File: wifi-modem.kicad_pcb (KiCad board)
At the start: 2 copper layers, 63.9 x 81.7 mm, 48 parts, among them J1 RS232, J2 Power, J3 Speaker, SW1 RESET, SW2 PROG, U1 ESP-12F, U2 MAX3238EAIT, U3 AMS1117-3.3

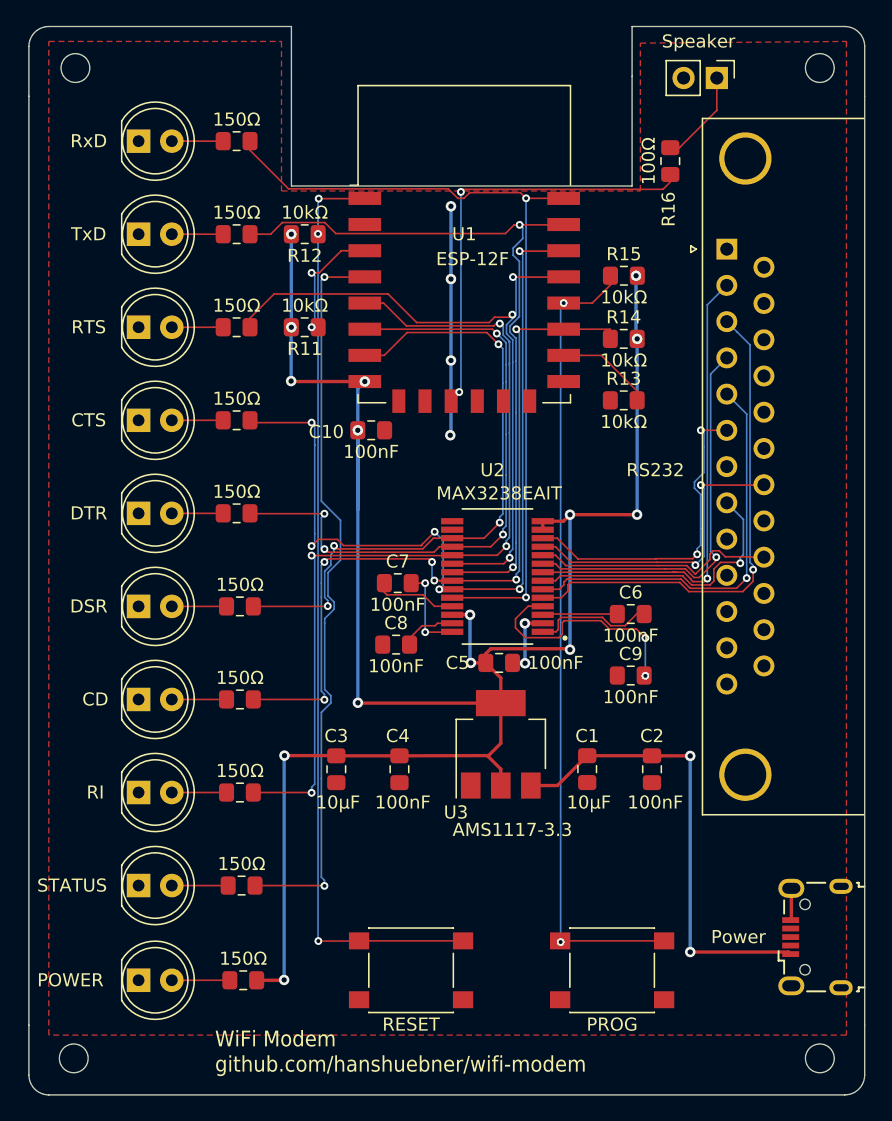
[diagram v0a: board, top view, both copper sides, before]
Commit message: Added LED drivers
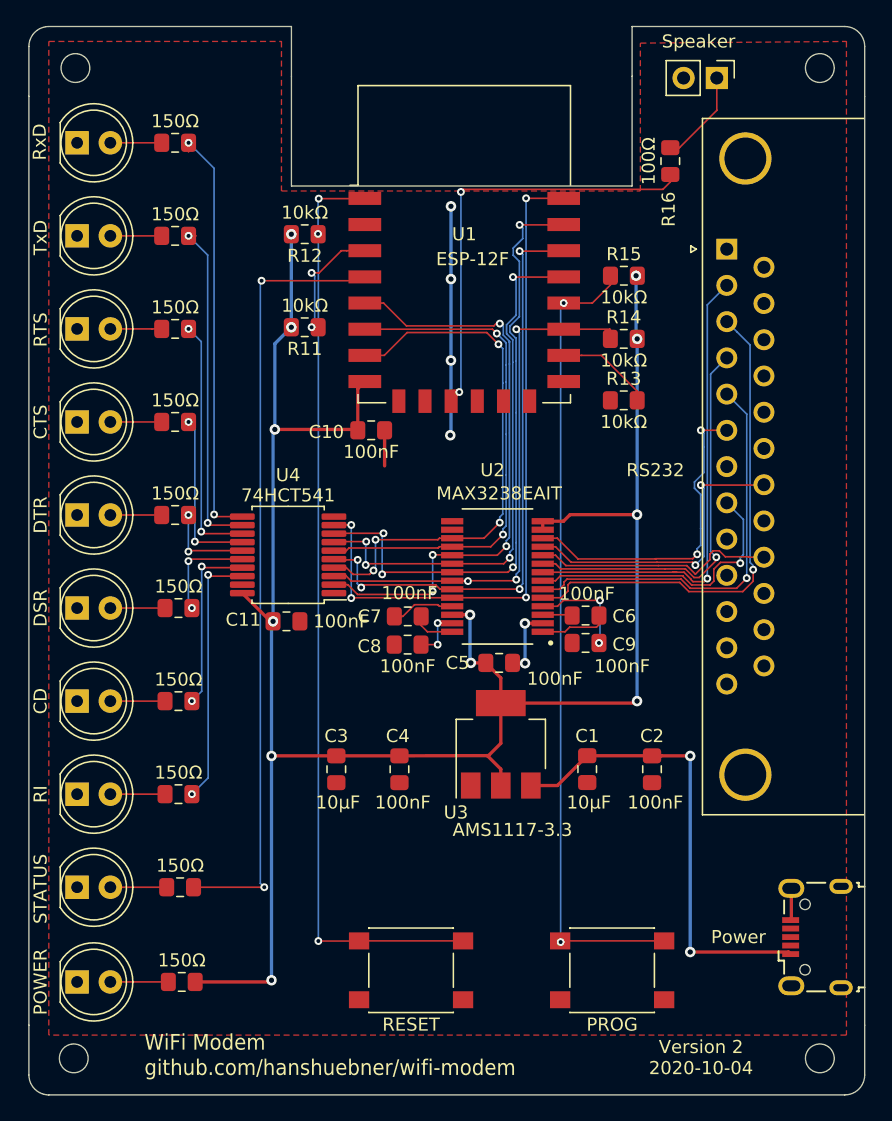
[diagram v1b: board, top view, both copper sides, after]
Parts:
- added C11: 100nF, Capacitor_SMD:C_0805_2012Metric_Pad1.15x1.40mm_HandSolder, F.Cu at (135.0, 105.0)
- added U4: 74HCT541, Package_SO:SSOP-20_5.3x7.2mm_P0.65mm, F.Cu at (135.1, 99.9)
- moved R10 4.70 mm to (127.0, 132.6)
- moved D1 4.70 mm to (119.0, 68.5)
- moved D2 4.70 mm to (119.0, 75.6)
- moved D3 4.70 mm to (119.0, 82.7)
- moved D4 4.70 mm to (119.0, 89.8)
- moved D5 4.70 mm to (119.0, 96.9)
- moved D6 4.70 mm to (119.0, 104.0)
- moved D7 4.70 mm to (119.0, 111.1)
- moved D8 4.70 mm to (119.0, 118.2)
- moved D9 4.70 mm to (119.0, 125.3)
- moved R1 4.70 mm to (126.5, 68.5)
- moved R2 4.70 mm to (126.5, 75.6)
- moved R3 4.70 mm to (126.5, 82.7)
- moved R4 4.70 mm to (126.5, 89.8)
- moved R5 4.70 mm to (126.5, 96.9)
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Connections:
- R7 pad 1: Net-(R14-Pad1) -> Net-(R7-Pad1)
- U1 pad 19: Net-(R3-Pad1) -> Net-(U1-Pad19)
- U1 pad 20: Net-(R4-Pad1) -> Net-(U1-Pad20)
- U1 pad 21: Net-(R2-Pad1) -> Net-(U1-Pad21)
- U1 pad 22: Net-(R1-Pad1) -> Net-(U1-Pad22)
- U1 pad 5: Net-(R8-Pad1) -> Net-(U1-Pad5)
- U1 pad 6: Net-(R5-Pad1) -> Net-(U1-Pad6)
- U1 pad 7: Net-(R6-Pad1) -> Net-(U1-Pad7)
- U2 pad 17: Net-(R6-Pad1) -> Net-(U1-Pad7)
- U2 pad 18: Net-(R5-Pad1) -> Net-(U1-Pad6)
- U2 pad 19: Net-(R8-Pad1) -> Net-(U1-Pad5)
- U2 pad 20: Net-(R3-Pad1) -> Net-(U1-Pad19)
- U2 pad 21: Net-(R2-Pad1) -> Net-(U1-Pad21)
- U2 pad 23: Net-(R4-Pad1) -> Net-(U1-Pad20)
- U2 pad 24: Net-(R1-Pad1) -> Net-(U1-Pad22)
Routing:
- net Net-(U1-Pad22): track 0.00 -> 53.7 mm, vias 0 -> 4
- net Net-(R4-Pad1): track 65.1 -> 13.2 mm, vias 6 -> 2
- net Net-(U1-Pad21): track 0.00 -> 48.0 mm, vias 0 -> 4
- net Net-(R8-Pad1): track 66.7 -> 19.9 mm, vias 4 -> 2
- net Net-(U1-Pad20): track 0.00 -> 45.8 mm, vias 0 -> 4
- net Net-(U1-Pad5): track 0.00 -> 45.3 mm, vias 0 -> 4
- net Net-(R5-Pad1): track 49.0 -> 6.98 mm, vias 4 -> 2
- net Net-(R6-Pad1): track 49.5 -> 7.88 mm, vias 4 -> 2
- net Net-(U1-Pad19): track 0.00 -> 41.6 mm, vias 0 -> 4
- net Net-(U1-Pad7): track 0.00 -> 41.0 mm, vias 0 -> 4
- net Net-(U1-Pad6): track 0.00 -> 39.4 mm, vias 0 -> 2
- net Net-(R3-Pad1): track 53.3 -> 19.1 mm, vias 3 -> 2
- net Net-(R2-Pad1): track 57.7 -> 25.8 mm
- net Net-(R1-Pad1): track 62.7 -> 32.1 mm
- net Net-(R14-Pad1): track 59.6 -> 42.6 mm, vias 6 -> 3
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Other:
- board text added: "Version 2 2020-10-04"

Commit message: PCB Version 3
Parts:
- added C12: 100nF, Capacitor_SMD:C_0805_2012Metric_Pad1.15x1.40mm_HandSolder, F.Cu at (130.9, 99.6)
- added C13: 100nF, Capacitor_SMD:C_0805_2012Metric_Pad1.15x1.40mm_HandSolder, F.Cu at (143.7, 99.7)
- added C14: 100nF, Capacitor_SMD:C_0805_2012Metric_Pad1.15x1.40mm_HandSolder, F.Cu at (137.3, 102.4)
- added R17: 1MΩ, Resistor_SMD:R_0805_2012Metric_Pad1.15x1.40mm_HandSolder, F.Cu at (130.9, 95.0)
- added R18: 1MΩ, Resistor_SMD:R_0805_2012Metric_Pad1.15x1.40mm_HandSolder, F.Cu at (143.8, 95.1)
- added U5: 74LV123, Package_SO:TSSOP-16_4.4x5mm_P0.65mm, F.Cu at (137.3, 98.1)
- U4: footprint Package_SO:SSOP-20_5.3x7.2mm_P0.65mm -> Package_SO:TSSOP-20_4.4x6.5mm_P0.65mm
- moved U4 11.0 mm to (137.3, 110.7)
- moved C11 10.8 mm to (137.3, 115.6)
- moved C7 8.56 mm to (149.0, 111.8)
- moved C8 8.56 mm to (149.0, 113.9)
- moved C6 8.35 mm to (162.1, 111.8)
- moved C9 8.35 mm to (162.1, 113.9)
- moved C1 7.82 mm to (155.4, 123.7)
- moved C2 7.82 mm to (160.4, 123.7)
- moved C3 7.82 mm to (136.2, 123.7)
- moved C4 7.82 mm to (141.1, 123.7)
- moved U3 7.82 mm to (148.8, 121.8)
- moved U2 5.75 mm to (155.5, 105.3)
- moved C5 5.75 mm to (155.7, 111.9)
- moved SW1 2.98 mm to (141.9, 133.1)
- moved SW2 2.98 mm to (157.3, 133.1)
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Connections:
- D1 pad 1: GND -> Net-(D1-Pad1)
- D1 pad 2: Net-(D1-Pad2) -> +3V3
- D2 pad 1: GND -> Net-(D2-Pad1)
- D2 pad 2: Net-(D2-Pad2) -> +3V3
- D3 pad 1: GND -> Net-(D3-Pad1)
- D3 pad 2: Net-(D3-Pad2) -> +3V3
- D4 pad 1: GND -> Net-(D4-Pad1)
- D4 pad 2: Net-(D4-Pad2) -> +3V3
- D5 pad 1: GND -> Net-(D5-Pad1)
- D5 pad 2: Net-(D5-Pad2) -> +3V3
- D6 pad 1: GND -> Net-(D6-Pad1)
- D6 pad 2: Net-(D6-Pad2) -> +3V3
- D7 pad 1: GND -> Net-(D7-Pad1)
- D7 pad 2: Net-(D7-Pad2) -> +3V3
- D8 pad 1: GND -> Net-(D8-Pad1)
- D8 pad 2: Net-(D8-Pad2) -> +3V3
- R1 pad 2: Net-(D1-Pad2) -> Net-(D1-Pad1)
- R2 pad 2: Net-(D2-Pad2) -> Net-(D2-Pad1)
- R3 pad 2: Net-(D3-Pad2) -> Net-(D3-Pad1)
- R4 pad 2: Net-(D4-Pad2) -> Net-(D4-Pad1)
- R5 pad 2: Net-(D5-Pad2) -> Net-(D5-Pad1)
- R6 pad 2: Net-(D6-Pad2) -> Net-(D6-Pad1)
- R7 pad 2: Net-(D7-Pad2) -> Net-(D7-Pad1)
- R8 pad 2: Net-(D8-Pad2) -> Net-(D8-Pad1)
- U4 pad 8: Net-(U1-Pad21) -> Net-(U4-Pad8)
- U4 pad 9: Net-(U1-Pad22) -> Net-(U4-Pad9)
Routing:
- net +3V3: track 161.8 -> 246.9 mm, vias 12 -> 25
- net Net-(U4-Pad8): track 0.00 -> 18.6 mm, vias 0 -> 2
- net Net-(R1-Pad1): track 32.1 -> 49.9 mm
- net Net-(R2-Pad1): track 25.8 -> 43.5 mm
- net Net-(R3-Pad1): track 19.1 -> 36.5 mm
- net Net-(R4-Pad1): track 13.2 -> 29.7 mm
- net Net-(R5-Pad1): track 6.98 -> 23.1 mm
- net Net-(U4-Pad9): track 0.00 -> 12.4 mm, vias 0 -> 2
- net Net-(C1-Pad1): track 36.7 -> 26.6 mm, vias 2 -> 0
- net Net-(U1-Pad19): track 41.6 -> 51.1 mm, vias 4 -> 3
- net Net-(C13-Pad1): track 0.00 -> 9.11 mm, vias 0 -> 2
- net Net-(R14-Pad1): track 42.6 -> 51.7 mm
- net Net-(R6-Pad1): track 7.88 -> 16.8 mm
- net Net-(C12-Pad1): track 0.00 -> 7.88 mm, vias 0 -> 2
- net Net-(C7-Pad1): track 4.84 -> 12.2 mm, vias 0 -> 2
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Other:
- net class Power: trace_width 0.254 -> 0.508
- board text added: "Standard C Value: 100nF Standard R Value: 10kΩ"
- board text added: "Version 3 2020-10-29"
- board text removed: "Version 2 2020-10-04"
